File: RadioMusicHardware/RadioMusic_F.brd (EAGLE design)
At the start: 107 x 19 mm, 30 parts, among them X1 VERT_SD_CARD

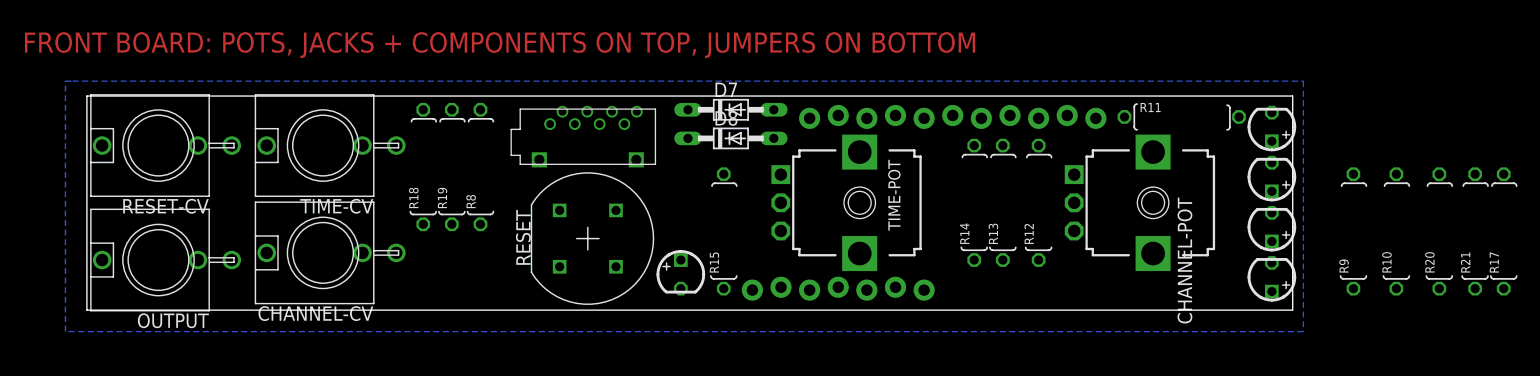
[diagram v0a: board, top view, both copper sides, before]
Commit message: Front board reworking
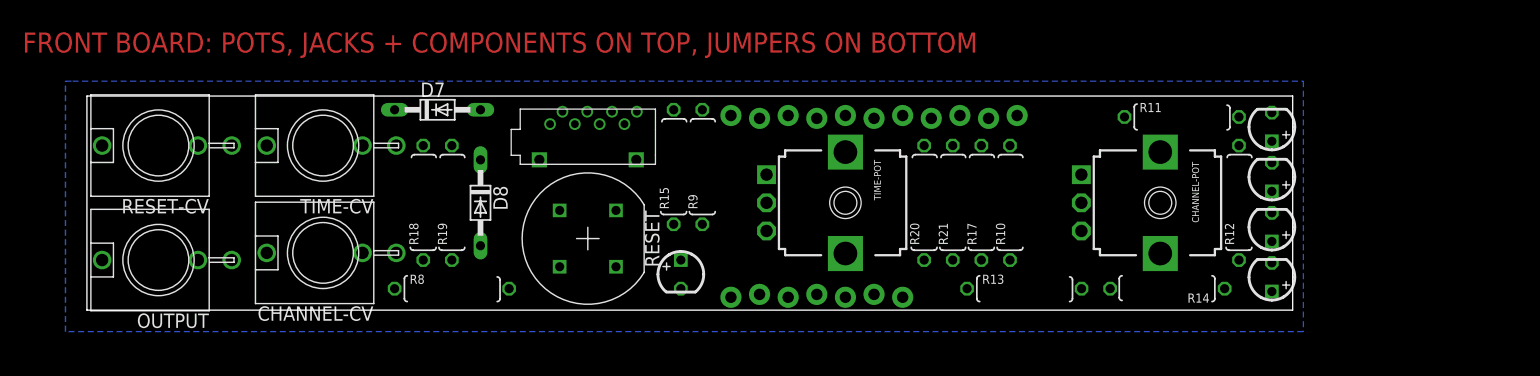
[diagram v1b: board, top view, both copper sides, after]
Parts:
- moved R9 58.1 mm to (54.6, 12.7)
- moved R17 46.4 mm to (79.4, 9.53)
- moved R21 46.4 mm to (76.8, 9.53)
- moved R20 45.8 mm to (74.3, 9.53)
- moved R10 34.4 mm to (81.9, 9.53)
- moved D7 26.0 mm to (31.1, 17.8)
- moved D8 22.9 mm to (34.9, 9.53), turned to 270 degrees
- moved R14 18.8 mm to (95.9, 1.91), turned to 180 degrees
- moved JP2 18.4 mm to (82.5, 17.1), turned to 0 degrees
- moved R12 17.8 mm to (102.2, 9.53)
- moved R8 11.1 mm to (32.4, 1.91), turned to 0 degrees
- moved R13 7.85 mm to (83.2, 1.91), turned to 0 degrees
- moved R15 7.24 mm to (52.1, 12.7)
- moved R18 3.17 mm to (29.8, 9.53)
- moved R19 3.17 mm to (32.4, 9.53)
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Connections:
- net GND_F: now also JP2.1, R8.1; no longer JP2.11, R8.2
- net LED1_F: now also JP2.2; no longer JP2.1
- net LED2_F: now also JP2.3; no longer JP2.2
- net LED3_F: now also JP2.4; no longer JP2.3
- net LED4_F: now also JP2.5; no longer JP2.4
- net LED_RESET_F: now also JP2.10; no longer JP2.9
- net MISO_F: now also JP2.11; no longer JP2.10
- net MOSI_F: now also JP2.6; no longer JP2.5
- net RESET_CV_F: now also JP2.8; no longer JP2.7
- net RESET_SW_F: now also JP2.7, R8.2; no longer JP2.6, R8.1
- net SS_F: now also JP2.9; no longer JP2.8

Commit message: Routed boards for checking
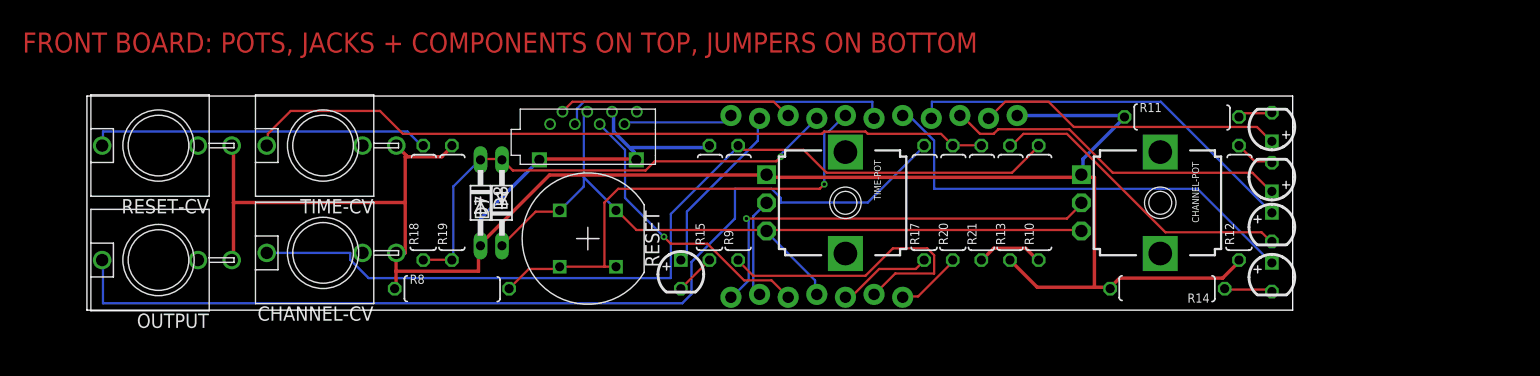
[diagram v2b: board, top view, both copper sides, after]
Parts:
- moved D7 10.0 mm to (36.8, 9.53), turned to 90 degrees
- moved R13 7.73 mm to (81.9, 9.53), turned to 90 degrees
- moved R17 5.08 mm to (74.3, 9.53)
- moved R15 4.49 mm to (55.2, 9.53)
- moved R9 4.49 mm to (57.8, 9.53)
- moved R21 2.54 mm to (79.4, 9.53)
- moved R10 2.54 mm to (84.5, 9.53)
- moved R20 2.54 mm to (76.8, 9.53)
- turned LED3 to 270 degrees
- turned LED4 to 270 degrees
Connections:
- net AUDIO_OUT_F: now also R17.1; no longer R17.2
- net CHANNEL_CV_F: now also R9.1; no longer R9.2
- net GND: now also R10.1, R21.1; no longer R10.2, R21.2
- net GND_F: now also R19.2; no longer R19.1
- net N$14: now also R18.2; no longer R18.1
- net N$3: now also R17.2; no longer R17.1
- net N$9: now also R10.2, R9.2; no longer R10.1, R9.1
- net RESET_CV_F: now also R18.1, R19.1; no longer R18.2, R19.2
- net TEMP: now also R20.2, R21.2; no longer R20.1, R21.1
- net TIME_CV_F: now also R20.1; no longer R20.2
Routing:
- net GND_F: track 0.00 -> 190.8 mm
- net N$3: track 0.00 -> 87.0 mm
- net N$9: track 0.00 -> 80.1 mm
- net +3.3V_F: track 0.00 -> 70.0 mm
- net TEMP: track 0.00 -> 66.7 mm
- net RESET_CV_F: track 0.00 -> 44.9 mm, vias 0 -> 1
- net RESET_SW_F: track 0.00 -> 43.4 mm, vias 0 -> 1
- net LED4_F: track 0.00 -> 40.7 mm
- net CHANNEL_POT_F: track 0.00 -> 38.1 mm, vias 0 -> 1
- net LED3_F: track 0.00 -> 35.8 mm
- net LED2_F: track 0.00 -> 30.8 mm
- net N$14: track 0.00 -> 30.2 mm
- net MOSI_F: track 0.00 -> 29.5 mm
- net N$20: track 0.00 -> 27.6 mm
- net LED1_F: track 0.00 -> 27.2 mm
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- removed copper zone on layer 16, net GND_F

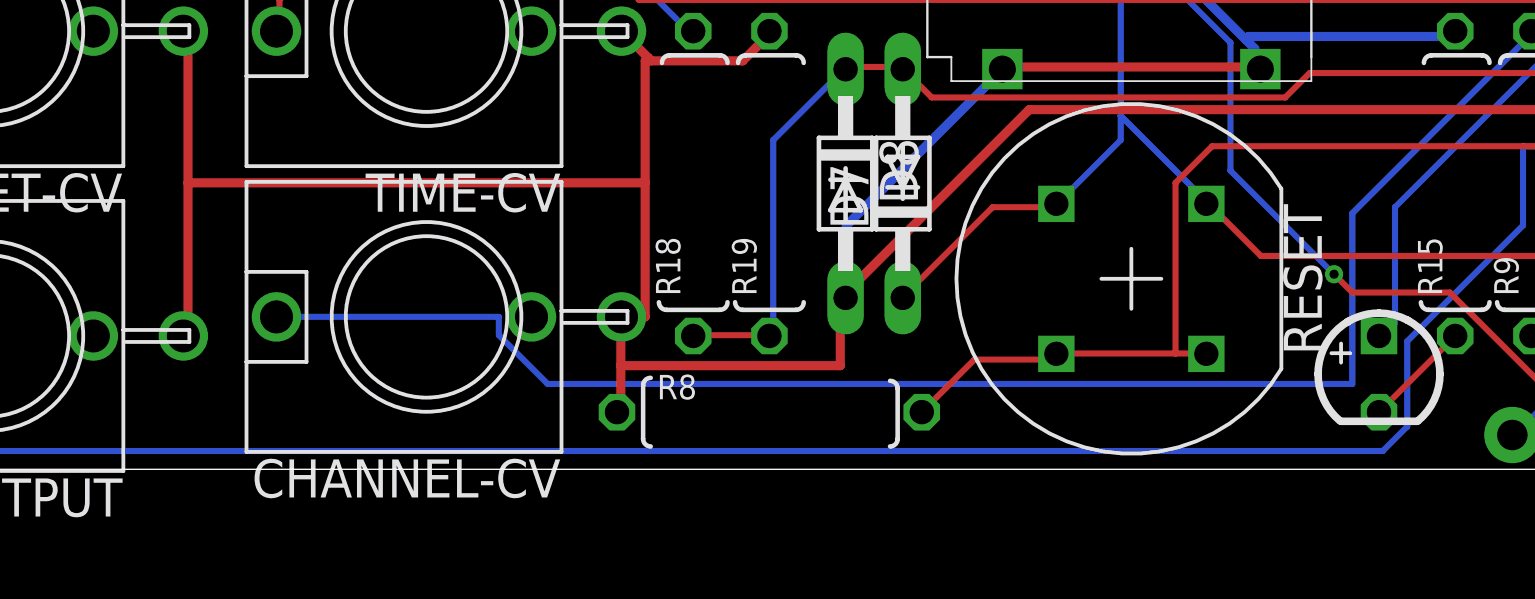
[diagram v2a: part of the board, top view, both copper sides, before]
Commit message: Create panel PCB, fix position CV socket position
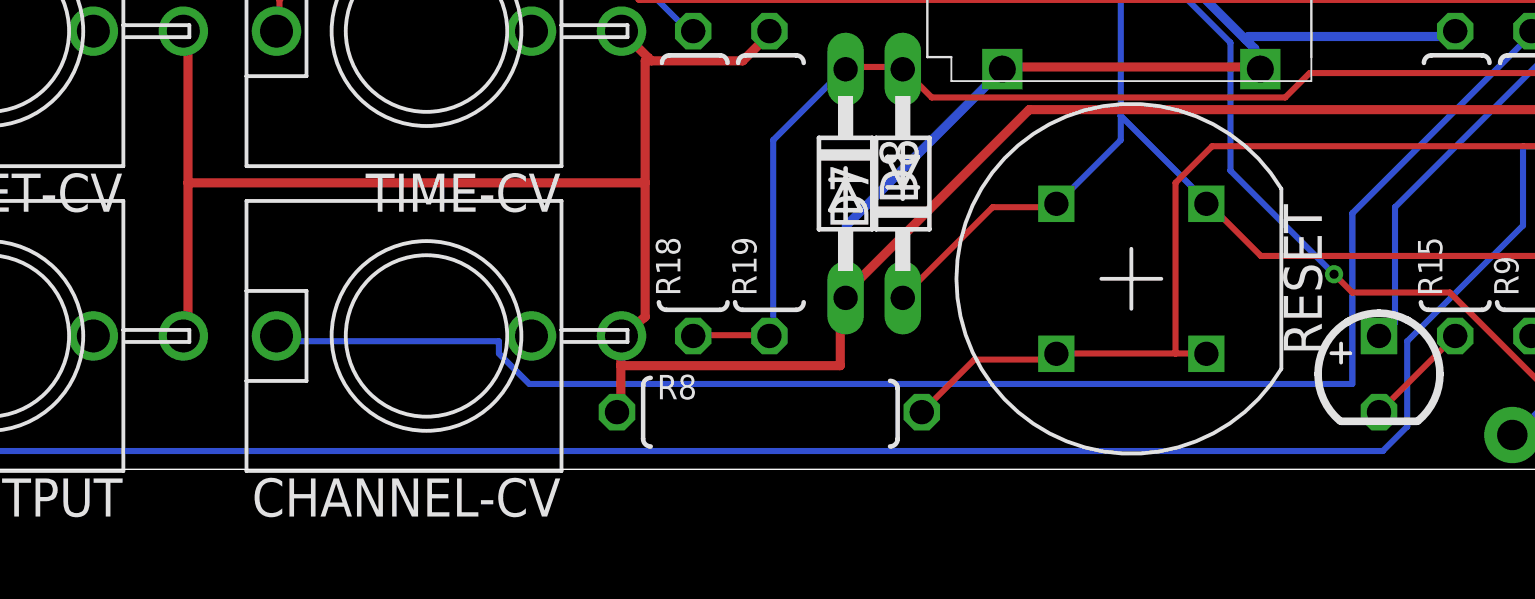
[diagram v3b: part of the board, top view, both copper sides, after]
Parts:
- moved CHANNEL-CV 0.63 mm to (21.0, 4.45)
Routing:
- net GND_F: track 190.8 -> 191.7 mm
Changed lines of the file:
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@@
 <attribute name="VALUE" x="90.83" y="11.485" size="0.6096" layer="27" rot="R270"/>
 </element>
-<element name="CHANNEL-CV" library="thonkiconn" package="WQP-PJ301M-12_JACK" value="" x="20.955" y="5.08" rot="R90"/>
+<element name="CHANNEL-CV" library="thonkiconn" package="WQP-PJ301M-12_JACK" value="" x="20.955" y="4.445" rot="R90"/>
 <element name="RESET-CV" library="thonkiconn" package="WQP-PJ301M-12_JACK" value="" x="6.35" y="14.605" rot="R90"/>
 <element name="OUTPUT" library="thonkiconn" package="WQP-PJ301M-12_JACK" value="" x="6.35" y="4.445" rot="R90"/>
@@
 <wire x1="27.432" y1="3.4544" x2="27.432" y2="2.032" width="0.3048" layer="1"/>
 <wire x1="27.432" y1="2.032" x2="27.305" y2="1.905" width="0.3048" layer="1"/>
-<wire x1="27.432" y1="5.08" x2="27.455" y2="5.08" width="0.3048" layer="1"/>
+<wire x1="27.432" y1="5.08" x2="27.455" y2="4.445" width="0.3048" layer="1"/>
 <wire x1="34.7472" y1="3.4544" x2="34.7472" y2="5.6896" width="0.3048" layer="1"/>
 <wire x1="27.432" y1="3.4544" x2="34.7472" y2="3.4544" width="0.3048" layer="1"/>
@@
 <wire x1="28.2448" y1="5.08" x2="28.2448" y2="9.5504" width="0.3048" layer="1"/>
 <wire x1="28.2448" y1="9.5504" x2="28.2448" y2="13.6144" width="0.3048" layer="1"/>
-<wire x1="27.455" y1="5.08" x2="28.2448" y2="5.08" width="0.3048" layer="1"/>
+<wire x1="27.455" y1="4.445" x2="28.2448" y2="5.08" width="0.3048" layer="1"/>
 <wire x1="28.2448" y1="13.6144" x2="28.3464" y2="13.716" width="0.3048" layer="1"/>
 <wire x1="28.2448" y1="9.5504" x2="13.0048" y2="9.5504" width="0.3048" layer="1"/>
@@
 <wire x1="57.912" y1="14.4272" x2="57.785" y2="14.605" width="0.2032" layer="1"/>
 <wire x1="84.328" y1="14.4272" x2="84.455" y2="14.605" width="0.2032" layer="1"/>
-<wire x1="23.368" y1="5.08" x2="15.955" y2="5.08" width="0.2032" layer="16"/>
-<wire x1="23.368" y1="4.4704" x2="23.368" y2="5.08" width="0.2032" layer="16"/>
-<wire x1="24.9936" y1="2.8448" x2="23.368" y2="4.4704" width="0.2032" layer="16"/>
-<wire x1="51.816" y1="2.8448" x2="24.9936" y2="2.8448" width="0.2032" layer="16"/>
+<wire x1="23.368" y1="4.2672" x2="16.0528" y2="4.2672" width="0.2032" layer="16"/>
+<wire x1="23.368" y1="3.8608" x2="23.368" y2="4.2672" width="0.2032" layer="16"/>
+<wire x1="24.384" y1="2.8448" x2="23.368" y2="3.8608" width="0.2032" layer="16"/>
+<wire x1="51.816" y1="2.8448" x2="24.384" y2="2.8448" width="0.2032" layer="16"/>
 <wire x1="51.816" y1="8.5344" x2="51.816" y2="2.8448" width="0.2032" layer="16"/>
 <wire x1="57.7088" y1="14.4272" x2="51.816" y2="8.5344" width="0.2032" layer="16"/>
+<wire x1="16.0528" y1="4.2672" x2="15.955" y2="4.445" width="0.2032" layer="16"/>
 <wire x1="57.7088" y1="14.4272" x2="57.785" y2="14.605" width="0.2032" layer="16"/>
 </signal>

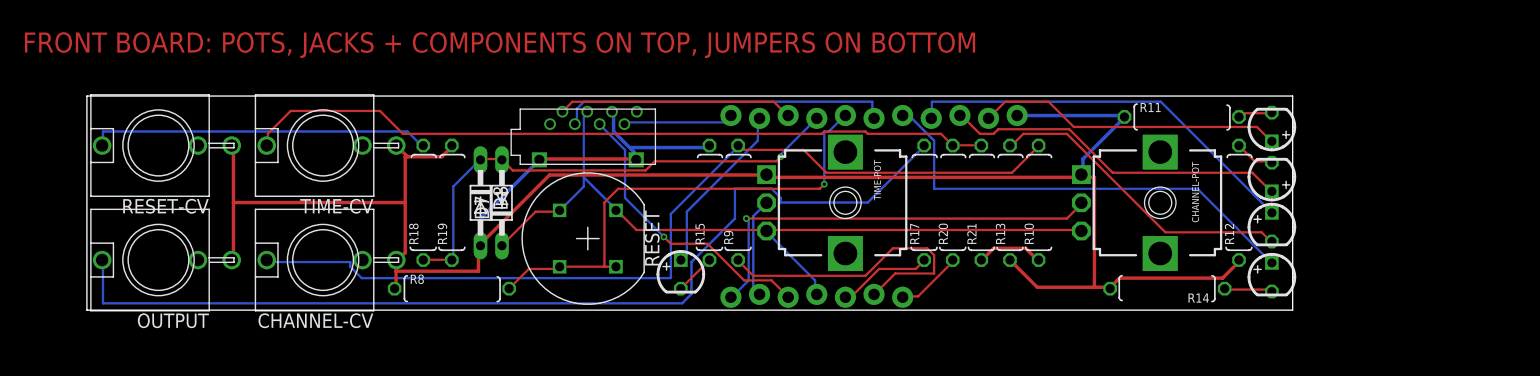
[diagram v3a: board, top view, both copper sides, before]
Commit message: Artwork on panels, notes on PCBs
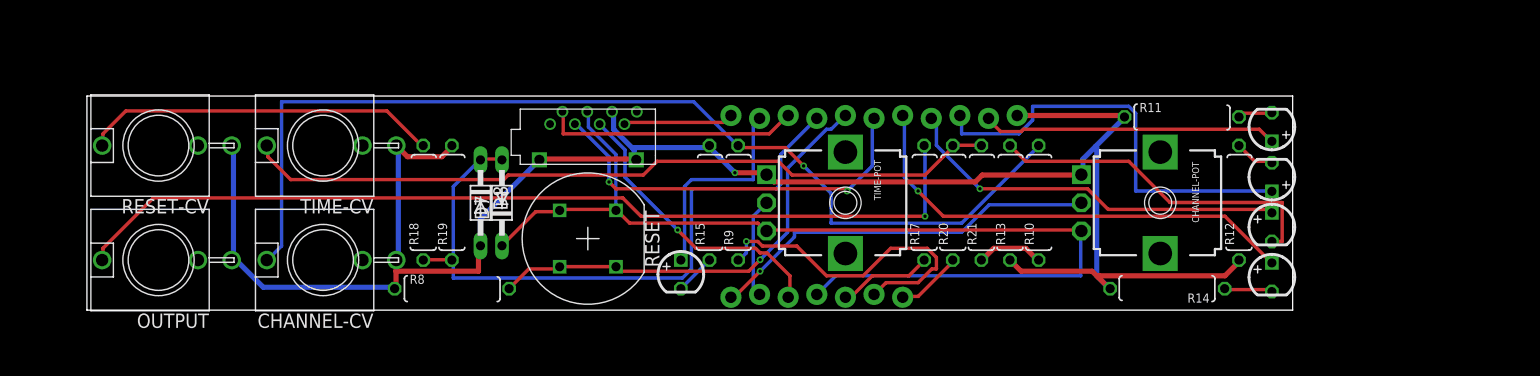
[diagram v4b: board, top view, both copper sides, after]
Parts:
- added U$1: (no value), TW_logos:MTM_2CM
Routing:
- net +3.3V_F: track 70.0 -> 91.6 mm
- net GND_F: track 191.7 -> 172.3 mm, vias 0 -> 1
- net RESET_CV_F: track 44.9 -> 60.0 mm, vias 1 -> 0
- net N$9: track 79.7 -> 90.7 mm, vias 0 -> 1
- net LED2_F: track 30.8 -> 38.2 mm
- net MOSI_F: track 29.5 -> 35.4 mm, vias 0 -> 2
- net N$3: track 87.0 -> 82.9 mm, vias 0 -> 1
- net RESET_SW_F: track 43.4 -> 39.9 mm
- net CHANNEL_POT_F: track 38.1 -> 34.8 mm
- net LED_RESET_F: track 15.5 -> 18.7 mm
- net N$20: track 27.6 -> 30.6 mm
- net CHANNEL_CV_F: track 27.0 -> 29.0 mm, vias 0 -> 1
- net SS_F: track 20.9 -> 22.6 mm
- net N$14: track 30.2 -> 31.6 mm
- net LED1_F: track 27.2 -> 26.2 mm
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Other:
- board text added: "ONLY JUMPER PINS ON THIS SIDE"
- board text added: "RadioMusic Front PCB rev 1 Designed in Herne Hill, London by Tom Whitwell October 2014 CC-BY-SA musicthing.co.uk"
- board text removed: "FRONT BOARD: POTS, JACKS + COMPONENTS ON TOP, JUMPERS ON BOTTOM"
